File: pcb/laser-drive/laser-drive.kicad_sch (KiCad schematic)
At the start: 29 parts, among them J1 CONN_01X03, P1 LaserOut, Q1 BCP5616Q, Q2 MTM232270, U2 MIC920

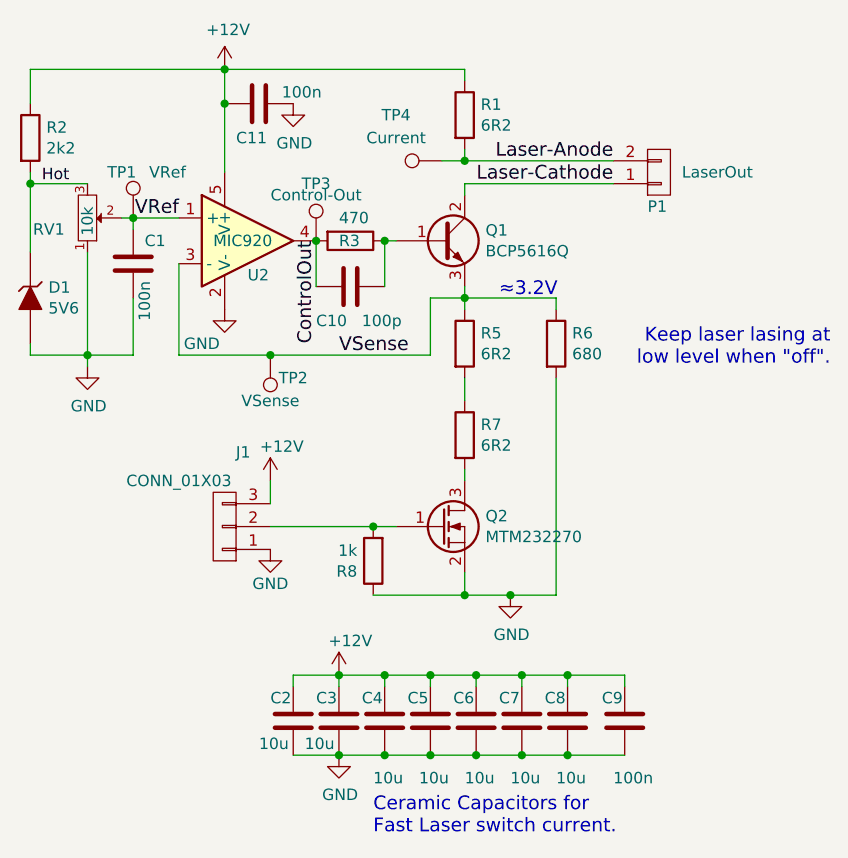
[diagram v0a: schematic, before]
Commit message: Update transistor that is out of production.
MTM232270 -> DMN2058UW
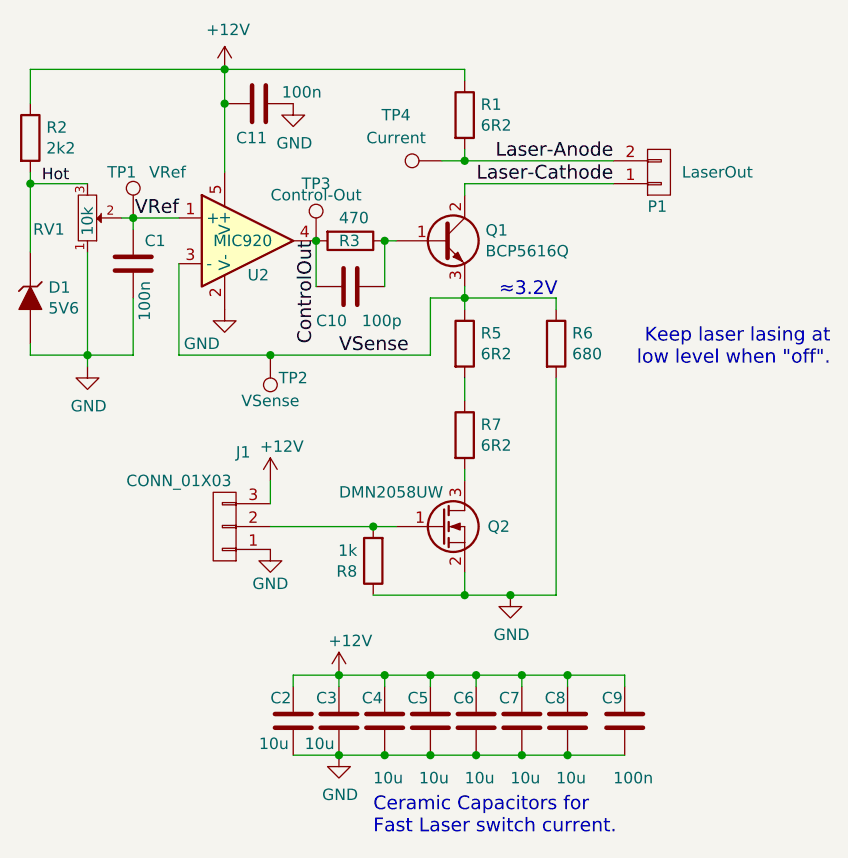
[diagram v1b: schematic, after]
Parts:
- Q2: value MTM232270 -> DMN2058UW
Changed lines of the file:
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@@
     (effects (font (size 1.524 1.524)) (justify left bottom))
   )
-  (label "ControlOut" (at 138.43 50.8 270)
+  (label "ControlOut" (at 138.43 50.8 270) (fields_autoplaced)
     (effects (font (size 1.524 1.524)) (justify right bottom))
   )
@@
     (effects (font (size 1.27 1.27)) (justify left bottom))
   )
-  (label "Laser-Anode" (at 171.45 41.91 180)
+  (label "Laser-Anode" (at 171.45 41.91 180) (fields_autoplaced)
     (effects (font (size 1.524 1.524)) (justify right bottom))
   )
-  (label "VSense" (at 140.97 63.5 0)
+  (label "VSense" (at 140.97 63.5 0) (fields_autoplaced)
     (effects (font (size 1.524 1.524)) (justify left bottom))
   )
-  (label "Laser-Cathode" (at 171.45 44.45 180)
+  (label "Laser-Cathode" (at 171.45 44.45 180) (fields_autoplaced)
     (effects (font (size 1.524 1.524)) (justify right bottom))
   )
-  (label "VRef" (at 123.19 48.26 180)
+  (label "VRef" (at 123.19 48.26 180) (fields_autoplaced)
     (effects (font (size 1.524 1.524)) (justify right bottom))
   )
@@
   (symbol (lib_id "laser-drive-rescue:Q_NMOS_GSD") (at 152.4 82.55 0) (unit 1)
     (in_bom yes) (on_board yes) (dnp no)
-    (property "Reference" "Q2" (at 157.2514 81.3816 0)
+    (property "Reference" "Q2" (at 157.48 82.55 0)
       (effects (font (size 1.27 1.27)) (justify left))
     )
-    (property "Value" "MTM232270" (at 157.2514 83.693 0)
+    (property "Value" "DMN2058UW" (at 140.97 78.74 0)
       (effects (font (size 1.27 1.27)) (justify left))
     )
@@
       (effects (font (size 1.27 1.27)) (justify left) hide)
     )
-    (property "Datasheet" "" (at 152.4 82.55 0)
-      (effects (font (size 1.27 1.27)))
+    (property "Datasheet" "https://www.diodes.com/assets/Datasheets/DMN2058UW.pdf" (at 152.4 82.55 0)
+      (effects (font (size 1.27 1.27)) hide)
     )
     (pin "1")
